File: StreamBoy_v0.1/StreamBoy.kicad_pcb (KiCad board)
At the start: 2 copper layers, 94 parts, among them IC1 LY68L6400SLIT, J1 GB-CART, Q1 SS8050-G, Q2 SS8050-G, U1 XC6SLX9-TQG144, U10 TPS62170DSG, U11 TPS62170DSG, U12 CP2102N-A01-GQFN28, U3 LSF0204PWR, U4 LSF0204PWR, U5 LSF0204PWR, U6 LSF0204PWR, U7 LSF0204PWR, U8 LSF0204PWR, U9 LSF0204PWR, X1 SG-7050CBN

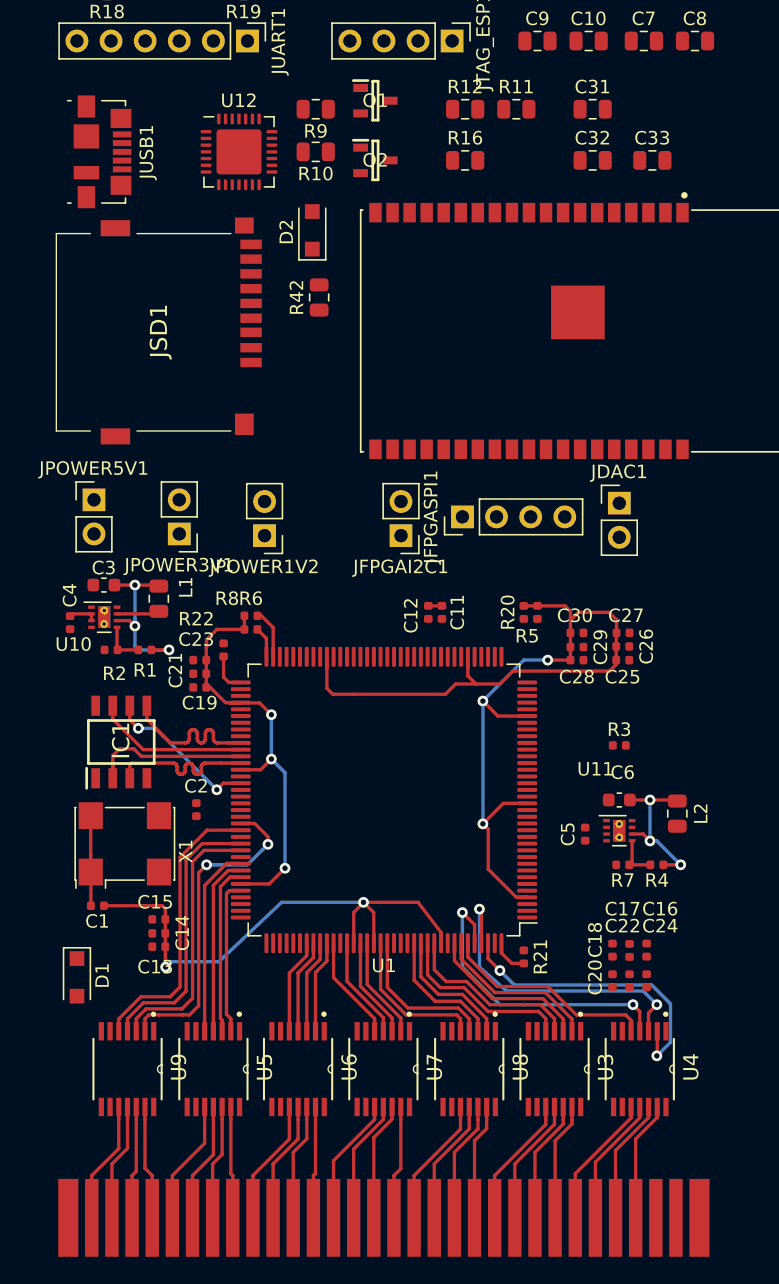
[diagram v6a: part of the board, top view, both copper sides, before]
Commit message: GB Reset fixed and moved some stuff
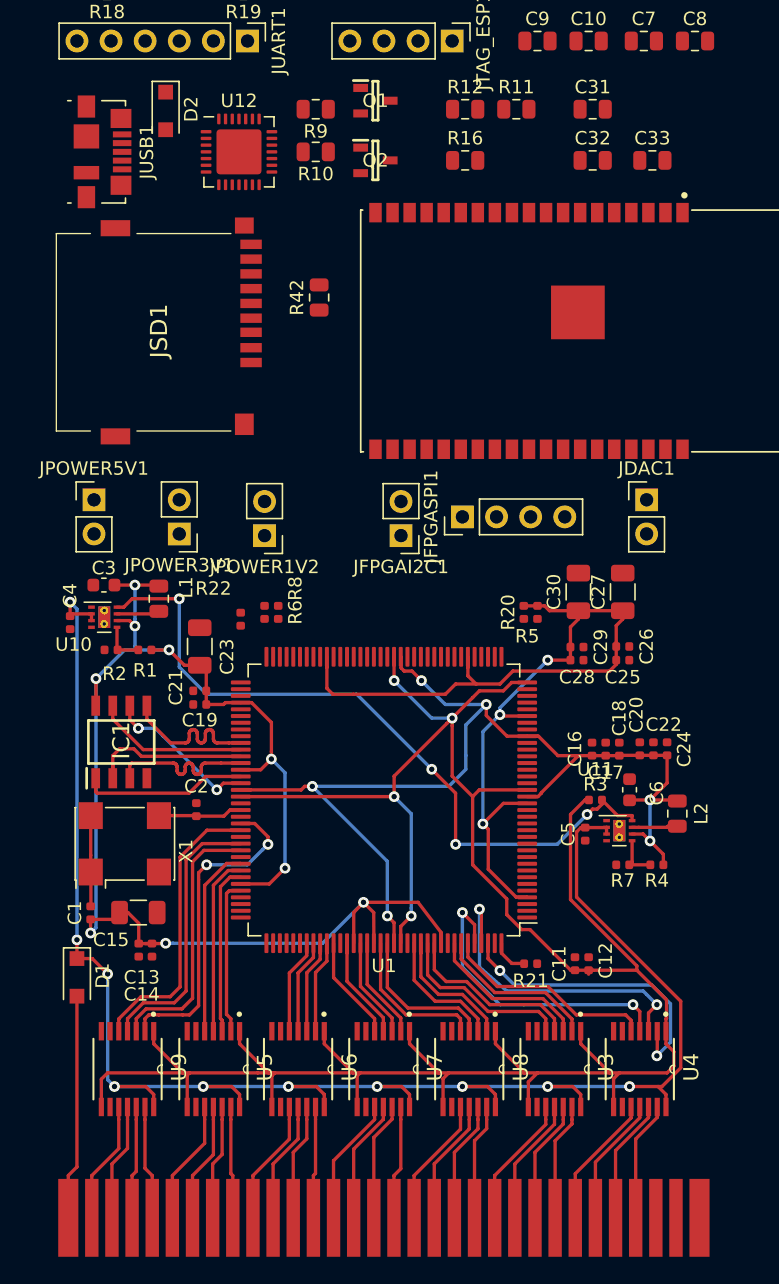
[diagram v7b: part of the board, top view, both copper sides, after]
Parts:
- C15, C23, C27, C30: footprint Capacitor_SMD:C_0402_1005Metric -> Capacitor_SMD:C_1206_3216Metric
- moved C12 28.8 mm to (61.0, 167.1), turned to 90 degrees
- moved C11 28.0 mm to (59.9, 167.1), turned to 90 degrees
- moved C17 17.3 mm to (62.2, 151.2), turned to 90 degrees
- moved C24 17.3 mm to (66.8, 151.1)
- moved C18 17.3 mm to (63.2, 151.2), turned to 90 degrees
- moved C16 15.5 mm to (61.2, 151.2), turned to 90 degrees
- moved C20 15.1 mm to (64.8, 151.1)
- moved C22 15.1 mm to (65.8, 151.1)
- moved D2 14.1 mm to (29.5, 103.6), turned to 270 degrees
- moved R3 4.44 mm to (61.5, 154.9)
- moved C30 3.05 mm to (60.2, 139.4), turned to 90 degrees
- moved C27 3.05 mm to (63.5, 139.4), turned to 90 degrees
- moved R22 2.62 mm to (35.1, 141.5)
- moved JDAC1 2.05 mm to (65.3, 132.6)
- moved R6 2.05 mm to (37.8, 141.0), turned to 90 degrees
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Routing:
- net VCC3: track 162.2 -> 366.5 mm, vias 11 -> 16
- net VCC5: track 2.16 -> 132.2 mm, vias 0 -> 10
- net VCC1V2: track 12.5 -> 80.2 mm, vias 3 -> 6
- net Net-(R3-Pad2): track 0.00 -> 53.8 mm, vias 0 -> 4
- net GB_5V: track 0.00 -> 16.8 mm
- net RAM_CS: track 0.00 -> 12.4 mm
- net FPGA_CLK_50M: track 0.00 -> 6.30 mm
- net FPGA_DONE: track 3.71 -> 0.00 mm
- net Net-(L2-Pad1): track 0.00 -> 3.40 mm
- net SUSPEND: track 2.99 -> 0.00 mm
- net Net-(R8-Pad2): track 2.32 -> 0.00 mm
